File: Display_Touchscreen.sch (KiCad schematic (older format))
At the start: 13 parts, among them U1 TSC2007

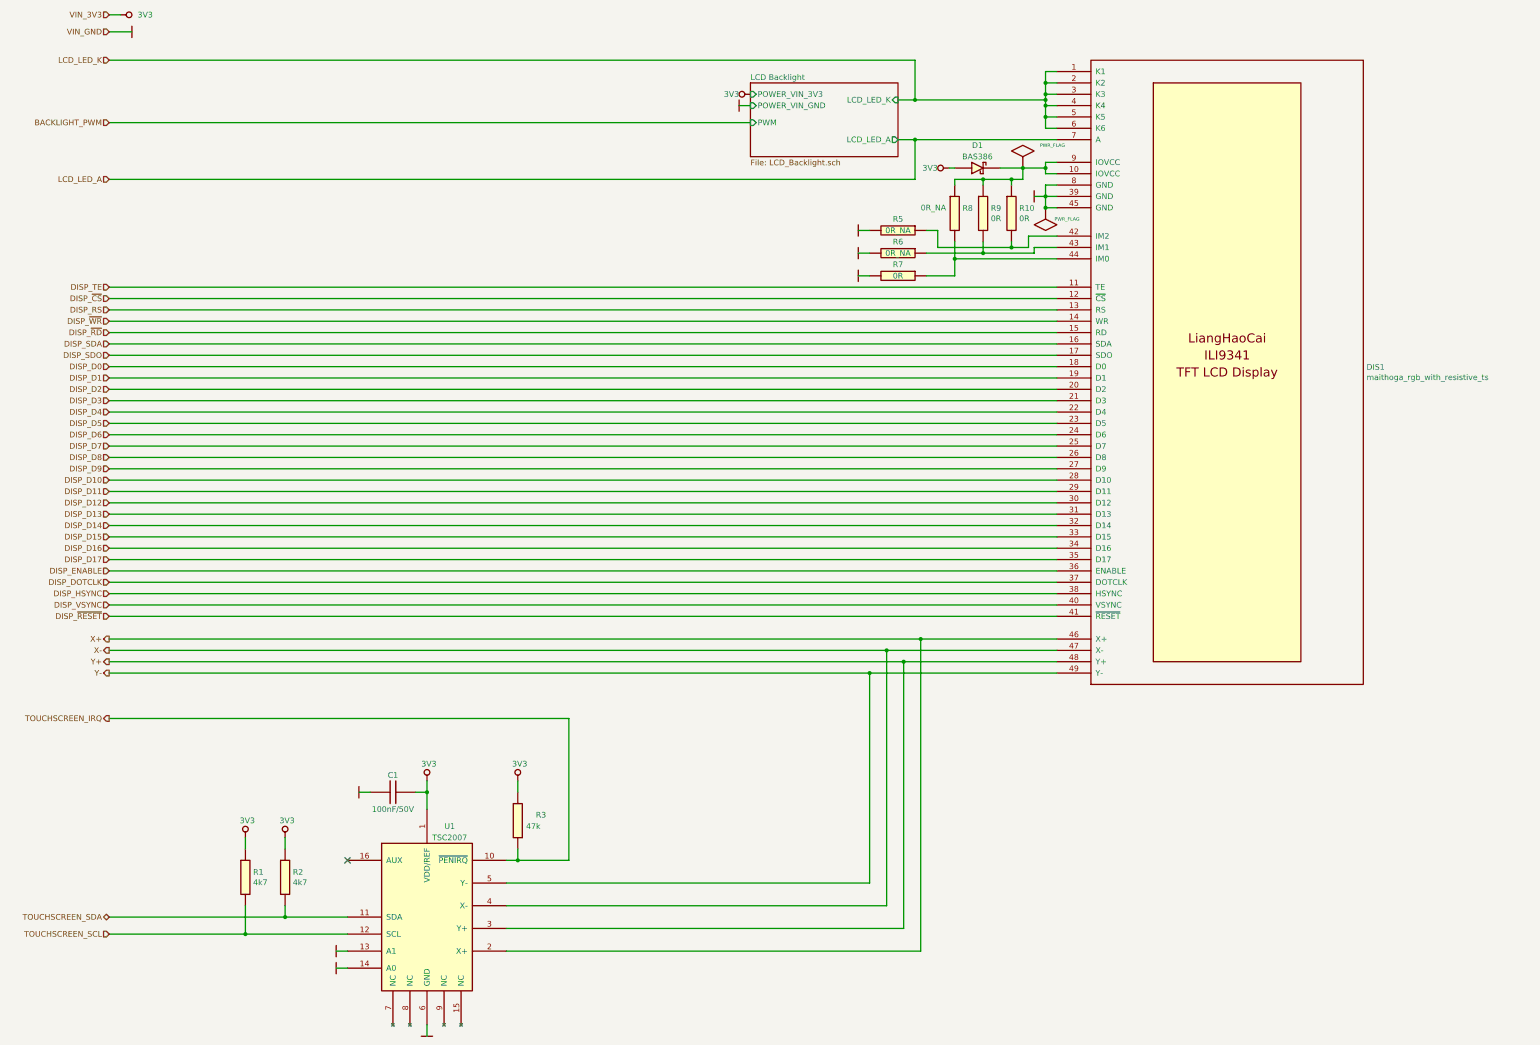
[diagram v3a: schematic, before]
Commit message: Added new capacitive display
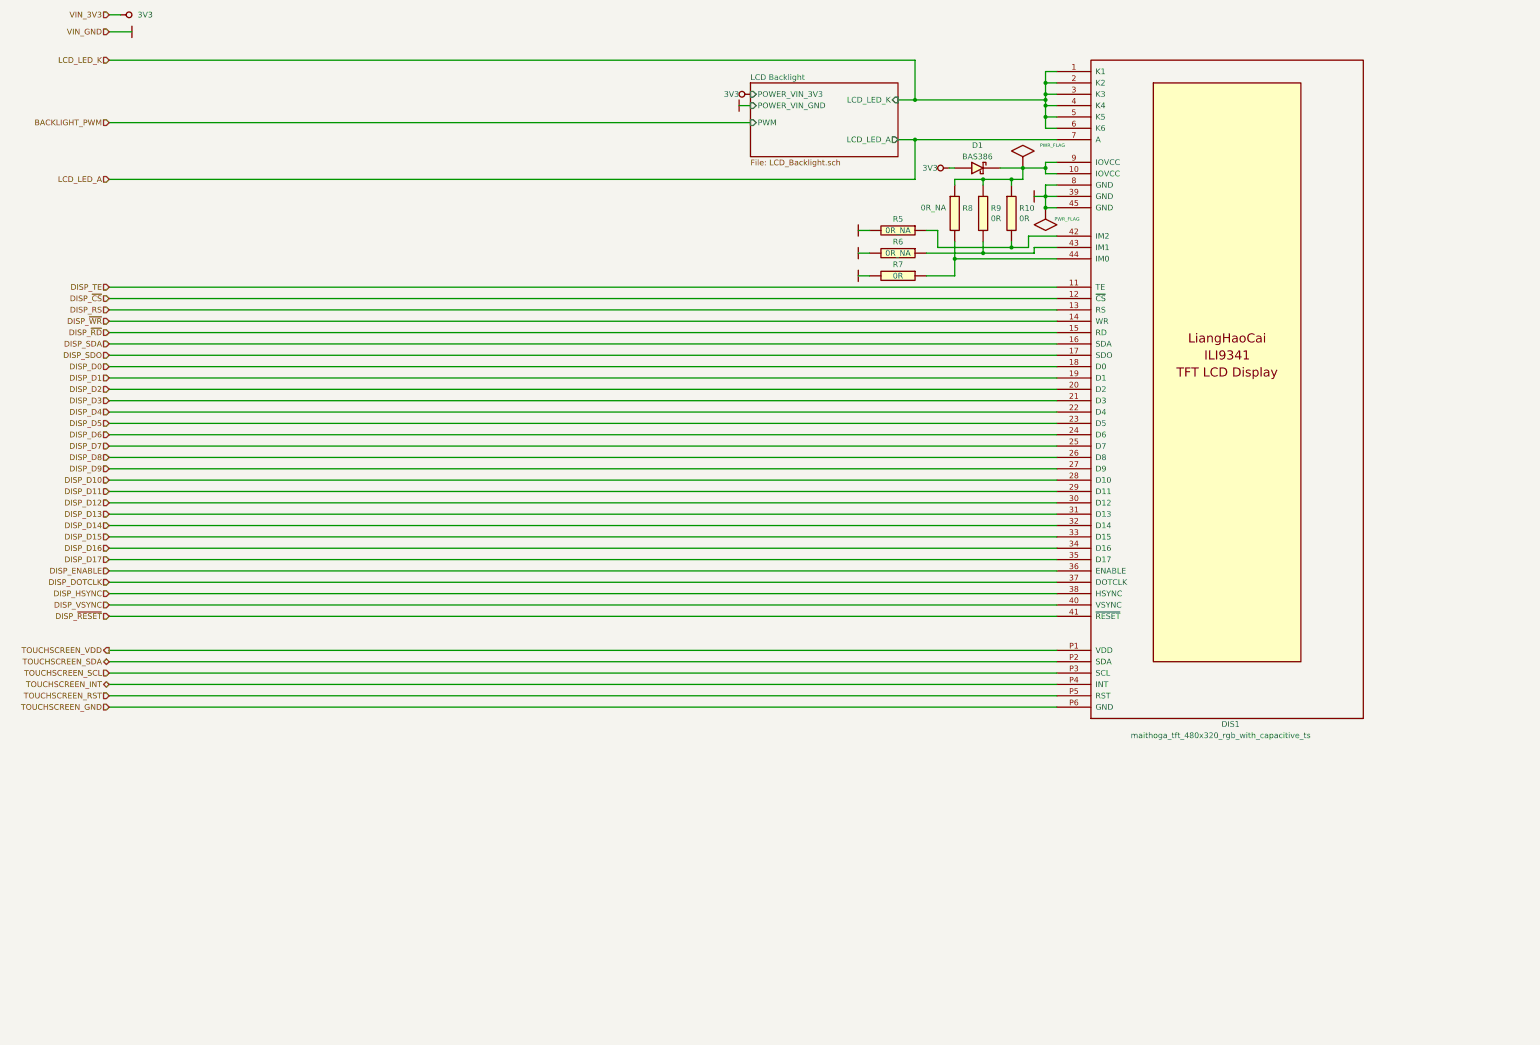
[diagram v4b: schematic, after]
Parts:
- removed C1: 100nF/50V, Capacitors_Smd_0603:100nF_0603, symbol Capacitors_Smd0603:100nF_0603
- removed DIS1: maithoga_rgb_with_resistive_ts, Display_Lcd:maithoga_tft_480x320_rgb_with_resistive_ts, symbol Display_Lcd:maithoga_tft_480x320_rgb_with_resistive_ts
- removed R1, R2: 4k7, Resistor_Smd_0603:4k7_0603, symbol Resistors_Smd0603:4k7_0603
- removed R3: 47k, Resistor_Smd_0603:47k_0603, symbol Resistors_Smd0603:47k_0603
- removed U1: TSC2007, Touch_Sensors:TSC2007_TSSOP16, symbol Touch_Sensors:TSC2007
- added DIS1: maithoga_tft_480x320_rgb_with_capacitive_ts, Display_Lcd:maithoga_tft_480x320_rgb_with_capacitive_ts, symbol Display_Lcd:maithoga_tft_480x320_rgb_with_capacitive_ts
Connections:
- net DISP_D0: now also DIS1.18 (D0)
- net DISP_D1: now also DIS1.19 (D1)
- net DISP_D10: now also DIS1.28 (D10)
- net DISP_D11: now also DIS1.29 (D11)
- net DISP_D12: now also DIS1.30 (D12)
- net DISP_D13: now also DIS1.31 (D13)
- net DISP_D14: now also DIS1.32 (D14)
- net DISP_D15: now also DIS1.33 (D15)
- net DISP_D16: now also DIS1.34 (D16)
- net DISP_D17: now also DIS1.35 (D17)
- net DISP_D2: now also DIS1.20 (D2)
- net DISP_D3: now also DIS1.21 (D3)
- net DISP_D4: now also DIS1.22 (D4)
- net DISP_D5: now also DIS1.23 (D5)
- net DISP_D6: now also DIS1.24 (D6)
- net DISP_D7: now also DIS1.25 (D7)
- net DISP_D8: now also DIS1.26 (D8)
- net DISP_D9: now also DIS1.27 (D9)
- net DISP_DOTCLK: now also DIS1.37 (DOTCLK)
- net DISP_ENABLE: now also DIS1.36 (ENABLE)
- net DISP_HSYNC: now also DIS1.38 (HSYNC)
- net DISP_RS: now also DIS1.13 (RS)
- net DISP_SDA: now also DIS1.16 (SDA)
- net DISP_SDO: now also DIS1.17 (SDO)
- net DISP_TE: now also DIS1.11 (TE)
- net DISP_VSYNC: now also DIS1.40 (VSYNC)
- net DISP_~CS~: now also DIS1.12 (~CS)
- net DISP_~RD~: now also DIS1.15 (RD)
- net DISP_~RESET~: now also DIS1.41 (~RESET)
- net DISP_~WR~: now also DIS1.14 (WR)
- net GND: now also DIS1.39 (GND), DIS1.45 (GND), DIS1.8 (GND)
- net LCD_LED_A: now also DIS1.7 (A)
- net LCD_LED_K: now also DIS1.1 (K1), DIS1.2 (K2), DIS1.3 (K3), DIS1.4 (K4), DIS1.5 (K5), DIS1.6 (K6)
- net TOUCHSCREEN_SCL: now also DIS1.P3 (SCL)
- net TOUCHSCREEN_SDA: now also DIS1.P2 (SDA)
- net at D1.2 (K), R10.1, R8.1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: now also DIS1.10 (IOVCC), DIS1.9 (IOVCC)
- net at R10.2, R5.1: now also DIS1.42 (IM2)
- net at R6.1, R9.2: now also DIS1.43 (IM1)
- net at R7.1, R8.2: now also DIS1.44 (IM0)
- new net TOUCHSCREEN_GND: DIS1.P6 (GND)
- new net TOUCHSCREEN_INT: DIS1.P4 (INT)
- new net TOUCHSCREEN_RST: DIS1.P5 (RST)
- new net TOUCHSCREEN_VDD: DIS1.P1 (VDD)
- no-connect marks 1 -> 0

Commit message: Generated gerbers
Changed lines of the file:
@@
 	11550 3100 11450 3100
 Connection ~ 11450 3100
+Wire Wire Line
+	3500 7350 11850 7350
+Wire Wire Line
+	3500 7450 11850 7450
+Wire Wire Line
+	3500 7550 11850 7550
+Wire Wire Line
+	3500 7650 11850 7650
+Text HLabel 3500 7550 0    50   Output ~ 0
+TOUCHSCREEN_INT
+Text HLabel 3500 7650 0    50   Input ~ 0
+TOUCHSCREEN_RST
+Text HLabel 3500 7750 0    50   Input ~ 0
+TOUCHSCREEN_GND
 $Comp
 L Display_Lcd:maithoga_tft_480x320_rgb_with_capacitive_ts DIS1
@@
 $EndComp
 Wire Wire Line
+	3500 7750 11850 7750
+Wire Wire Line
 	3500 7250 11850 7250
-Wire Wire Line
-	3500 7350 11850 7350
-Wire Wire Line
-	3500 7450 11850 7450
-Wire Wire Line
-	3500 7550 11850 7550
-Wire Wire Line
-	3500 7650 11850 7650
-Wire Wire Line
-	3500 7750 11850 7750
-Text HLabel 3500 7550 0    50   BiDi ~ 0
-TOUCHSCREEN_INT
-Text HLabel 3500 7650 0    50   Input ~ 0
-TOUCHSCREEN_RST
-Text HLabel 3500 7750 0    50   Input ~ 0
-TOUCHSCREEN_GND
 $EndSCHEMATC
